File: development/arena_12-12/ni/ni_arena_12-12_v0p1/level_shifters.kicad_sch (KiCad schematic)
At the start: 225 parts, among them U10 TXB0108PW, U11 TXB0108PW, U12 TXB0108PW, U13 TXB0108PW, U14 TXB0108PW, U15 TXB0108PW, U16 TXB0108PW, U17 TXB0108PW, U18 TXB0108PW, U19 74LVC2G17, U2 TXB0108PW, U20 74LVC2G17, U21 74LVC2G17, U22 74LVC2G17, U23 74LVC2G17, U24 74LVC2G17, U25 74LVC2G17, U26 74LVC2G17, U27 74LVC2G17, U28 74LVC2G17, U29 74LVC2G17, U3 TXB0108PW, U30 74LVC2G17, U31 74LVC2G17, U32 74LVC2G17, U33 74LVC2G17, U34 74LVC2G17, U35 74LVC2G17, U36 74LVC2G17, U37 74LVC2G17, U38 74LVC2G17, U4 TXB0108PW, U5 TXB0108PW, U6 TXB0108PW, U7 TXB0108PW, U8 TXB0108PW, U9 TXB0108PW

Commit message: Worked on layout for 12-12 ni arena with schmitt buffers.
Finished layout of components at base of panel columns.
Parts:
- renumbered R112 to R100, R113 to R101, R114 to R102, R115 to R103, R116 to R104, R117 to R105, R118 to R106, R119 to R107, R120 to R108, R121 to R109, R122 to R110, R123 to R111, R124 to R112, R125 to R113, R126 to R114, R127 to R115, R128 to R116, R129 to R117, R130 to R118, R131 to R119, R132 to R120, R133 to R121, R134 to R122, R135 to R123, R136 to R124, R137 to R125, R138 to R126, R139 to R127, R140 to R128, R141 to R129, R142 to R130, R143 to R131, R144 to R132, R145 to R133, R146 to R134, R147 to R135, R148 to R136, R149 to R137, R150 to R138, R151 to R139, R152 to R140, R153 to R141, R154 to R142, R155 to R143, R156 to R144, R157 to R145, R158 to R146, R159 to R147, R160 to R148, R161 to R149, R162 to R150, R163 to R151, R164 to R152, R165 to R153, R166 to R154, R167 to R155, R168 to R156, R173 to R157, R174 to R158, R169 to R159, R170 to R160, R171 to R161, R172 to R162, R41 to R29, R42 to R30, R43 to R31, R44 to R32, R45 to R33, R46 to R34, R47 to R35, R48 to R36, R49 to R37, R50 to R38, R51 to R39, R52 to R40, R53 to R41, R54 to R42, R55 to R43, R56 to R44, R57 to R45, R58 to R46, R59 to R47, R60 to R48, R61 to R49, R62 to R50, R63 to R51, R64 to R52, R65 to R53, R66 to R54, R67 to R55, R68 to R56, R69 to R57, R70 to R58, R71 to R59, R72 to R60, R73 to R61, R74 to R62, R75 to R63, R76 to R64, R77 to R65, R78 to R66, R79 to R67, R80 to R68, R81 to R69, R82 to R70, R83 to R71, R84 to R72, R85 to R73, R86 to R74, R87 to R75, R88 to R76, R89 to R77, R90 to R78, R91 to R79, R92 to R80, R93 to R81, R94 to R82, R95 to R83, R96 to R84, R97 to R85, R98 to R86, R99 to R87, R100 to R88, R101 to R89, R102 to R90, R103 to R91, R104 to R92, R105 to R93, R106 to R94, R107 to R95, R108 to R96, R109 to R97, R110 to R98, R111 to R99

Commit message: Worked on layout for 12-12 NI arena /w schmitt buffers.
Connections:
- net +3.3V: no longer C28.1, C29.1, C30.1, C31.1, C32.1, C33.1, U28.5 (VCC), U29.5 (VCC), U30.5 (VCC), U31.5 (VCC), U36.5 (VCC), U37.5 (VCC)
- net +5V: now also C28.1, C29.1, C30.1, C31.1, C32.1, C33.1, U28.5 (VCC), U29.5 (VCC), U30.5 (VCC), U31.5 (VCC), U36.5 (VCC), U37.5 (VCC)
- net PAN5V.MISO_08: now also U36.3; no longer U36.1
- net PAN5V.MISO_09: now also U36.1; no longer U36.3
- net PAN5V.MISO_10: now also U37.3; no longer U37.1
- net PAN5V.MISO_11: now also U37.1; no longer U37.3
- net at U37.4: now also U18.17 (B3); no longer U18.16 (B4)
- net at U37.6: now also U18.16 (B4); no longer U18.17 (B3)
- net at U18.18 (B2): now also U36.6; no longer U36.4
- net at U18.20 (B1): now also U36.4; no longer U36.6
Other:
- moved on the sheet: U36A, U36B, U37A, U37B

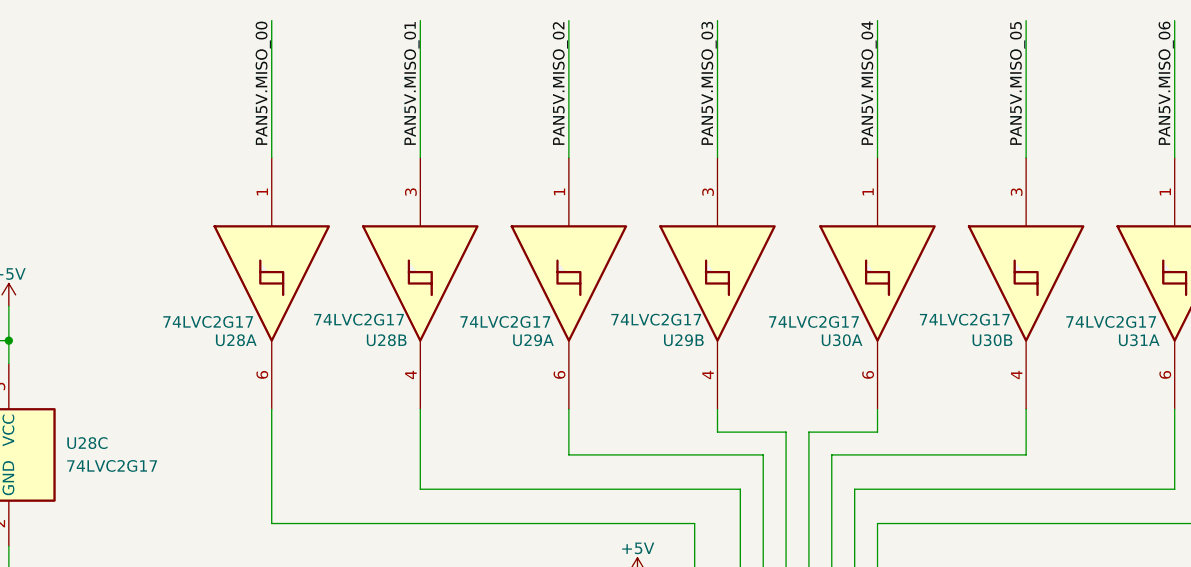
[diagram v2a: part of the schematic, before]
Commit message: Worked on layout of 12-12 NI arena with schmitt buffers.
Finished preliminary layout.
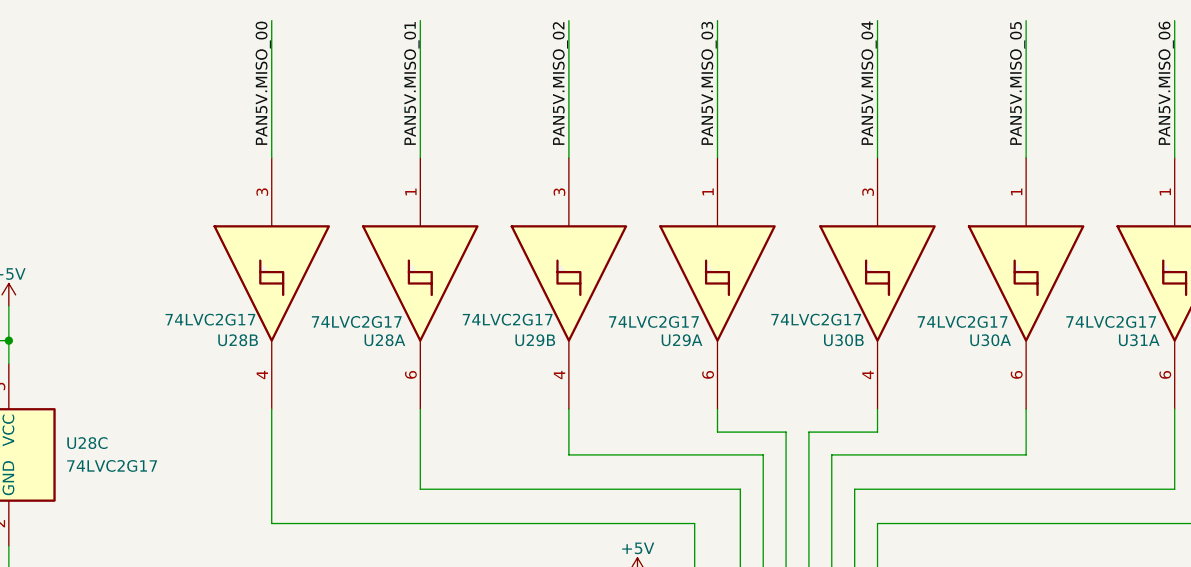
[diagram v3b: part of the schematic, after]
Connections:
- net PAN5V.MISO_00: now also U28.3; no longer U28.1
- net PAN5V.MISO_01: now also U28.1; no longer U28.3
- net PAN5V.MISO_02: now also U29.3; no longer U29.1
- net PAN5V.MISO_03: now also U29.1; no longer U29.3
- net PAN5V.MISO_04: now also U30.3; no longer U30.1
- net PAN5V.MISO_05: now also U30.1; no longer U30.3
- net at U28.6: now also U17.18 (B2); no longer U17.20 (B1)
- net at U30.6: now also U17.14 (B6); no longer U17.15 (B5)
- net at U28.4: now also U17.20 (B1); no longer U17.18 (B2)
- net at U29.6: now also U17.16 (B4); no longer U17.17 (B3)
- net at U30.4: now also U17.15 (B5); no longer U17.14 (B6)
- net at U29.4: now also U17.17 (B3); no longer U17.16 (B4)
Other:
- moved on the sheet: U28A, U28B, U29A, U29B, U30A, U30B
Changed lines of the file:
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@@
 	(symbol
 		(lib_id "74xGxx:74LVC2G17")
-		(at 351.79 396.24 90)
+		(at 368.3 396.24 90)
 		(mirror x)
 		(unit 1)
@@
 		(dnp no)
 		(property "Reference" "U28"
-			(at 345.44 401.32 90)
+			(at 361.95 401.32 90)
 			(effects
 				(font
@@
 		)
 		(property "Value" "74LVC2G17"
-			(at 339.598 399.288 90)
+			(at 356.108 399.288 90)
 			(effects
 				(font
@@
 		)
 		(property "Footprint" "Package_TO_SOT_SMD:SOT-23-6"
-			(at 351.79 396.24 0)
+			(at 368.3 396.24 0)
 			(effects
 				(font
@@
 		)
 		(property "Datasheet" "http://www.ti.com/lit/sg/scyt129e/scyt129e.pdf"
-			(at 351.79 396.24 0)
+			(at 368.3 396.24 0)
 			(effects
 				(font
@@
 		)
 		(property "Description" "Dual Buffer Schmitt Triggered, Low-Voltage CMOS"
-			(at 351.79 396.24 0)
+			(at 368.3 396.24 0)
 			(effects
 				(font
@@
 	(symbol
 		(lib_id "74xGxx:74LVC2G17")
-		(at 419.1 396.24 90)
+		(at 435.61 396.24 90)
 		(mirror x)
 		(unit 1)
@@
 		(dnp no)
 		(property "Reference" "U30"
-			(at 412.75 401.32 90)
+			(at 429.26 401.32 90)
 			(effects
 				(font
@@
 		)
 		(property "Value" "74LVC2G17"
-			(at 406.908 399.288 90)
+			(at 423.418 399.288 90)
 			(effects
 				(font
@@
 		)
 		(property "Footprint" "Package_TO_SOT_SMD:SOT-23-6"
-			(at 419.1 396.24 0)
+			(at 435.61 396.24 0)
 			(effects
 				(font
@@
 		)
 		(property "Datasheet" "http://www.ti.com/lit/sg/scyt129e/scyt129e.pdf"
-			(at 419.1 396.24 0)
+			(at 435.61 396.24 0)
 			(effects
 				(font
@@
 		)
 		(property "Description" "Dual Buffer Schmitt Triggered, Low-Voltage CMOS"
-			(at 419.1 396.24 0)
+			(at 435.61 396.24 0)
 			(effects
 				(font
@@
 	(symbol
 		(lib_id "74xGxx:74LVC2G17")
-		(at 368.3 396.24 90)
+		(at 351.79 396.24 90)
 		(mirror x)
 		(unit 2)
@@
 		(dnp no)
 		(property "Reference" "U28"
-			(at 362.204 401.32 90)
+			(at 345.694 401.32 90)
 			(effects
 				(font
@@
 		)
 		(property "Value" "74LVC2G17"
-			(at 356.362 399.034 90)
+			(at 339.852 399.034 90)
 			(effects
 				(font
@@
 		)
 		(property "Footprint" "Package_TO_SOT_SMD:SOT-23-6"
-			(at 368.3 396.24 0)
+			(at 351.79 396.24 0)
 			(effects
 				(font
@@
 		)
 		(property "Datasheet" "http://www.ti.com/lit/sg/scyt129e/scyt129e.pdf"
-			(at 368.3 396.24 0)
+			(at 351.79 396.24 0)
 			(effects
 				(font
@@
 		)
 		(property "Description" "Dual Buffer Schmitt Triggered, Low-Voltage CMOS"
-			(at 368.3 396.24 0)
+			(at 351.79 396.24 0)
 			(effects
 				(font
@@
 	(symbol
 		(lib_id "74xGxx:74LVC2G17")
-		(at 384.81 396.24 90)
+		(at 401.32 396.24 90)
 		(mirror x)
 		(unit 1)
@@
 		(dnp no)
 		(property "Reference" "U29"
-			(at 378.46 401.32 90)
+			(at 394.97 401.32 90)
 			(effects
 				(font
@@
 		)
 		(property "Value" "74LVC2G17"
-			(at 372.618 399.288 90)
+			(at 389.128 399.288 90)
 			(effects
 				(font
@@
 		)
 		(property "Footprint" "Package_TO_SOT_SMD:SOT-23-6"
-			(at 384.81 396.24 0)
+			(at 401.32 396.24 0)
 			(effects
 				(font
@@
 		)
 		(property "Datasheet" "http://www.ti.com/lit/sg/scyt129e/scyt129e.pdf"
-			(at 384.81 396.24 0)
+			(at 401.32 396.24 0)
 			(effects
 				(font
@@
 		)
 		(property "Description" "Dual Buffer Schmitt Triggered, Low-Voltage CMOS"
-			(at 384.81 396.24 0)
+			(at 401.32 396.24 0)
 			(effects
 				(font
@@
 	(symbol
 		(lib_id "74xGxx:74LVC2G17")
-		(at 435.61 396.24 90)
+		(at 419.1 396.24 90)
 		(mirror x)
 		(unit 2)
@@
 		(dnp no)
 		(property "Reference" "U30"
-			(at 429.514 401.32 90)
+			(at 413.004 401.32 90)
 			(effects
 				(font
@@
 		)
 		(property "Value" "74LVC2G17"
-			(at 423.672 399.034 90)
+			(at 407.162 399.034 90)
 			(effects
 				(font
@@
 		)
 		(property "Footprint" "Package_TO_SOT_SMD:SOT-23-6"
-			(at 435.61 396.24 0)
+			(at 419.1 396.24 0)
 			(effects
 				(font
@@
 		)
 		(property "Datasheet" "http://www.ti.com/lit/sg/scyt129e/scyt129e.pdf"
-			(at 435.61 396.24 0)
+			(at 419.1 396.24 0)
 			(effects
 				(font
@@
 		)
 		(property "Description" "Dual Buffer Schmitt Triggered, Low-Voltage CMOS"
-			(at 435.61 396.24 0)
+			(at 419.1 396.24 0)
 			(effects
 				(font
@@
 	(symbol
 		(lib_id "74xGxx:74LVC2G17")
-		(at 401.32 396.24 90)
+		(at 384.81 396.24 90)
 		(mirror x)
 		(unit 2)
@@
 		(dnp no)
 		(property "Reference" "U29"
-			(at 395.224 401.32 90)
+			(at 378.714 401.32 90)
 			(effects
 				(font
@@
 		)
 		(property "Value" "74LVC2G17"
-			(at 389.382 399.034 90)
+			(at 372.872 399.034 90)
 			(effects
 				(font
@@
 		)
 		(property "Footprint" "Package_TO_SOT_SMD:SOT-23-6"
-			(at 401.32 396.24 0)
+			(at 384.81 396.24 0)
 			(effects
 				(font
@@
 		)
 		(property "Datasheet" "http://www.ti.com/lit/sg/scyt129e/scyt129e.pdf"
-			(at 401.32 396.24 0)
+			(at 384.81 396.24 0)
 			(effects
 				(font
@@
 		)
 		(property "Description" "Dual Buffer Schmitt Triggered, Low-Voltage CMOS"
-			(at 401.32 396.24 0)
+			(at 384.81 396.24 0)
 			(effects
 				(font

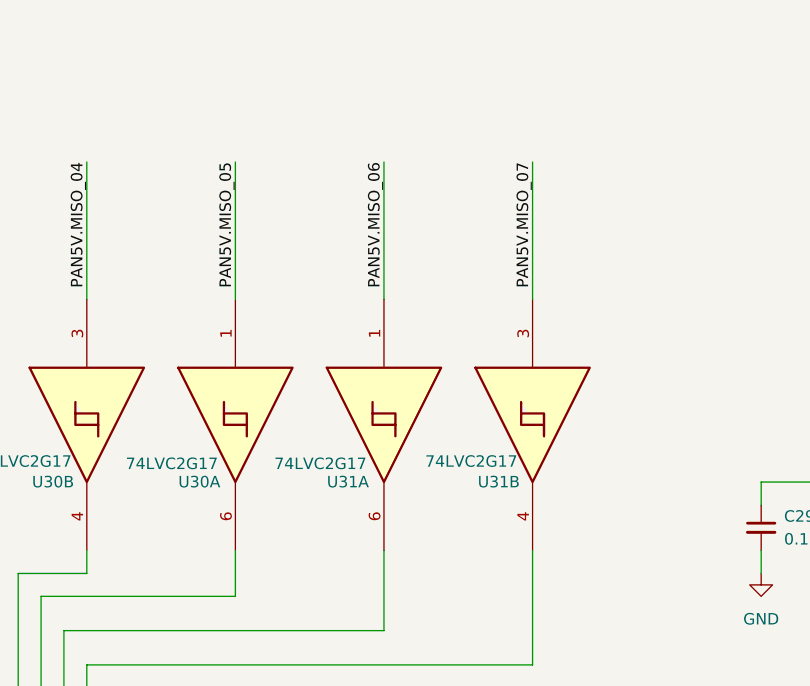
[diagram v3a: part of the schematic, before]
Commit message: Worked on routing 12-12 NI arena.
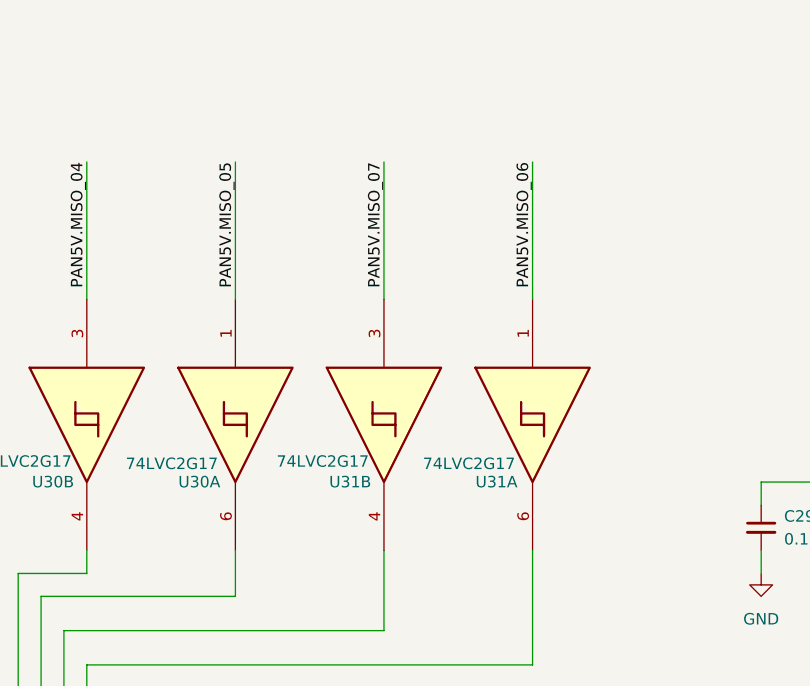
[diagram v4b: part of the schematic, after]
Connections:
- net at U31.4: now also U17.13 (B7); no longer U17.12 (B8)
- net at U31.6: now also U17.12 (B8); no longer U17.13 (B7)
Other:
- moved on the sheet: U31A, U31B
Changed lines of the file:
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@@
 	(wire
 		(pts
-			(xy 468.63 381) (xy 468.63 365.76)
+			(xy 452.12 381) (xy 452.12 365.76)
 		)
 		(stroke
@@
 	(wire
 		(pts
-			(xy 452.12 381) (xy 452.12 365.76)
+			(xy 468.63 381) (xy 468.63 365.76)
 		)
 		(stroke
@@
 	)
 	(label "PAN5V.MISO_07"
-		(at 468.63 365.76 270)
+		(at 452.12 365.76 270)
 		(fields_autoplaced yes)
 		(effects
@@
 	)
 	(label "PAN5V.MISO_06"
-		(at 452.12 365.76 270)
+		(at 468.63 365.76 270)
 		(fields_autoplaced yes)
 		(effects
@@
 	(symbol
 		(lib_id "74xGxx:74LVC2G17")
-		(at 468.63 396.24 90)
+		(at 452.12 396.24 90)
 		(mirror x)
 		(unit 2)
@@
 		(dnp no)
 		(property "Reference" "U31"
-			(at 462.534 401.32 90)
+			(at 446.024 401.32 90)
 			(effects
 				(font
@@
 		)
 		(property "Value" "74LVC2G17"
-			(at 456.692 399.034 90)
+			(at 440.182 399.034 90)
 			(effects
 				(font
@@
 		)
 		(property "Footprint" "Package_TO_SOT_SMD:SOT-23-6"
-			(at 468.63 396.24 0)
+			(at 452.12 396.24 0)
 			(effects
 				(font
@@
 		)
 		(property "Datasheet" "http://www.ti.com/lit/sg/scyt129e/scyt129e.pdf"
-			(at 468.63 396.24 0)
+			(at 452.12 396.24 0)
 			(effects
 				(font
@@
 		)
 		(property "Description" "Dual Buffer Schmitt Triggered, Low-Voltage CMOS"
-			(at 468.63 396.24 0)
+			(at 452.12 396.24 0)
 			(effects
 				(font
@@
 	(symbol
 		(lib_id "74xGxx:74LVC2G17")
-		(at 452.12 396.24 90)
+		(at 468.63 396.24 90)
 		(mirror x)
 		(unit 1)
@@
 		(dnp no)
 		(property "Reference" "U31"
-			(at 445.77 401.32 90)
+			(at 462.28 401.32 90)
 			(effects
 				(font
@@
 		)
 		(property "Value" "74LVC2G17"
-			(at 439.928 399.288 90)
+			(at 456.438 399.288 90)
 			(effects
 				(font
@@
 		)
 		(property "Footprint" "Package_TO_SOT_SMD:SOT-23-6"
-			(at 452.12 396.24 0)
+			(at 468.63 396.24 0)
 			(effects
 				(font
@@
 		)
 		(property "Datasheet" "http://www.ti.com/lit/sg/scyt129e/scyt129e.pdf"
-			(at 452.12 396.24 0)
+			(at 468.63 396.24 0)
 			(effects
 				(font
@@
 		)
 		(property "Description" "Dual Buffer Schmitt Triggered, Low-Voltage CMOS"
-			(at 452.12 396.24 0)
+			(at 468.63 396.24 0)
 			(effects
 				(font
